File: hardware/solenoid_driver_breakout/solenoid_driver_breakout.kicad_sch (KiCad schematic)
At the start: 24 parts, among them J1 DC IN, J2 CONTROL, J3 Solenoid, Q1 PMV40UN2R, Q2 PMV40UN2R

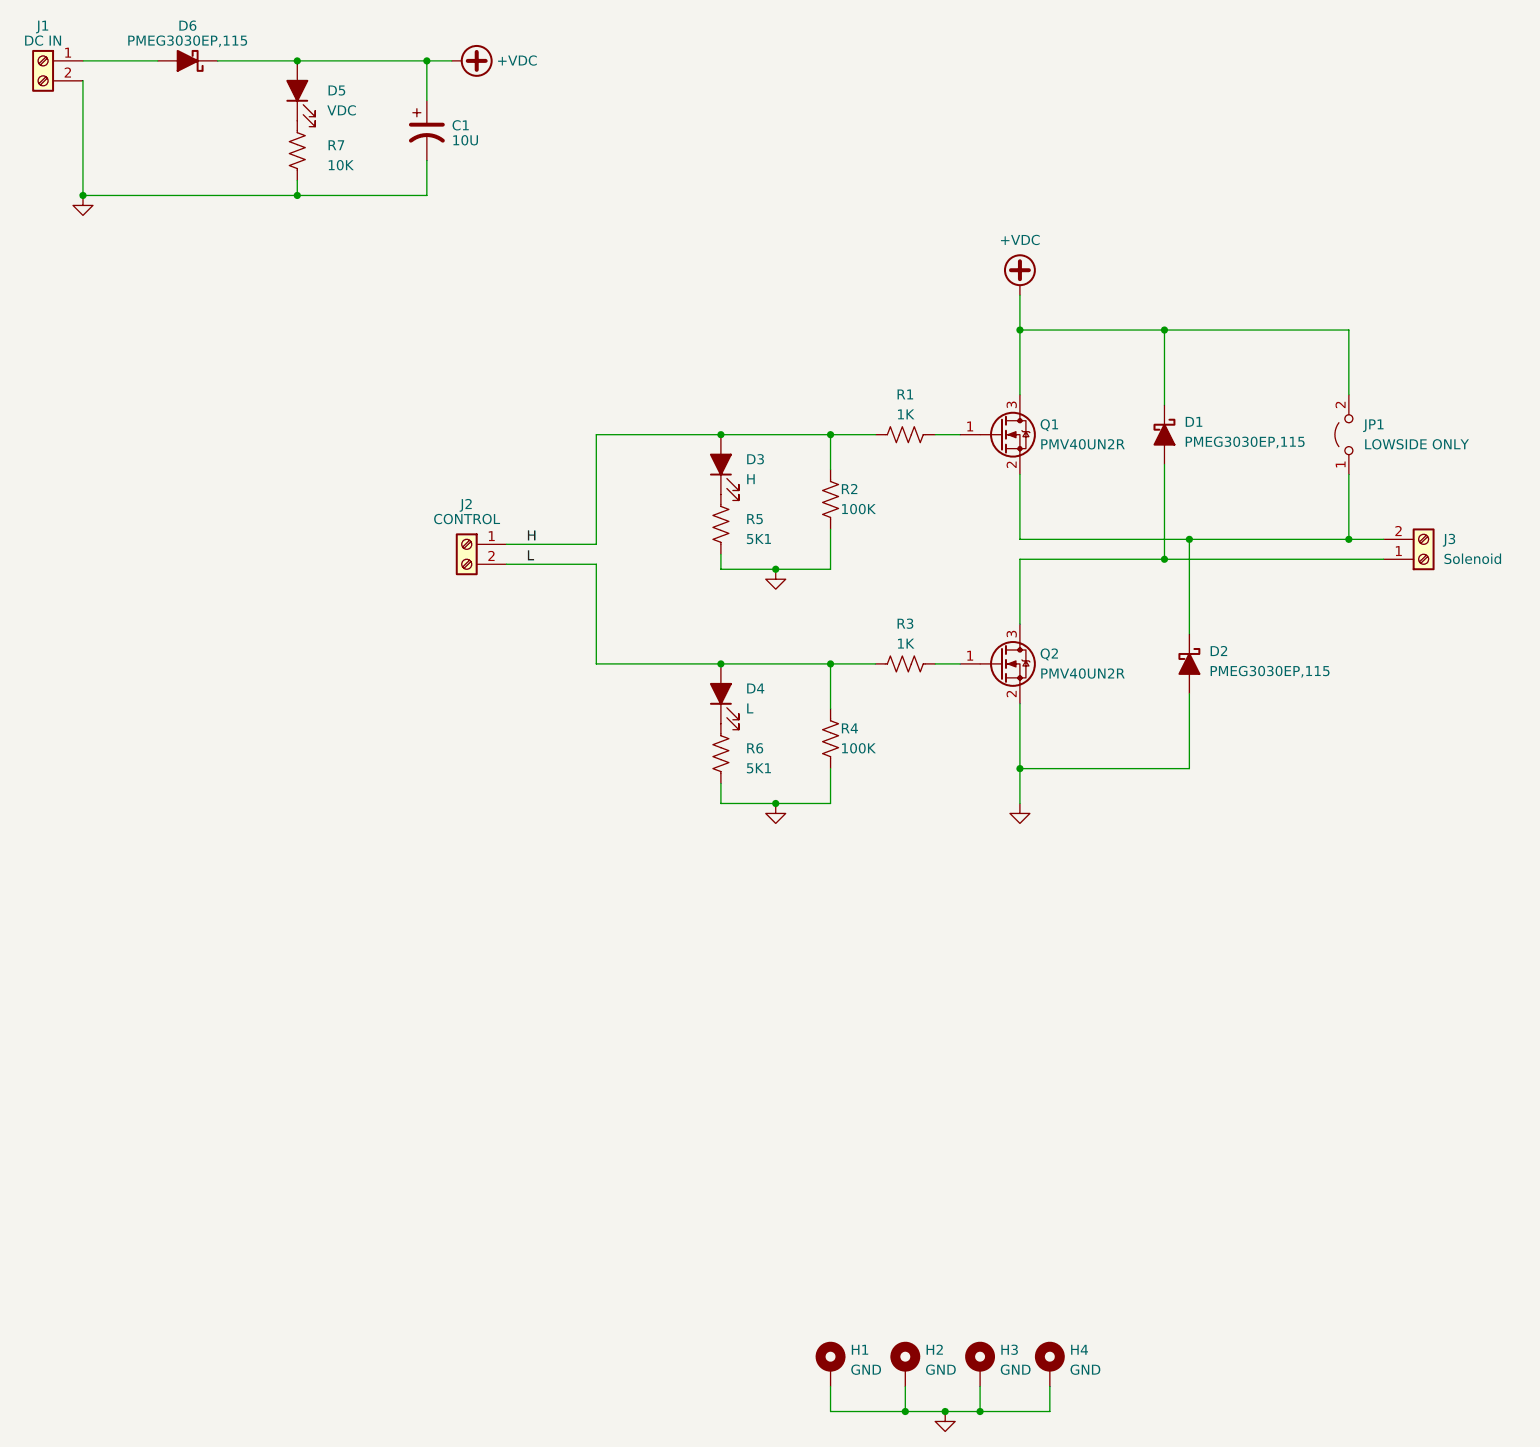
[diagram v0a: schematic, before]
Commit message: Switch solenoid driver to dual low-side switches
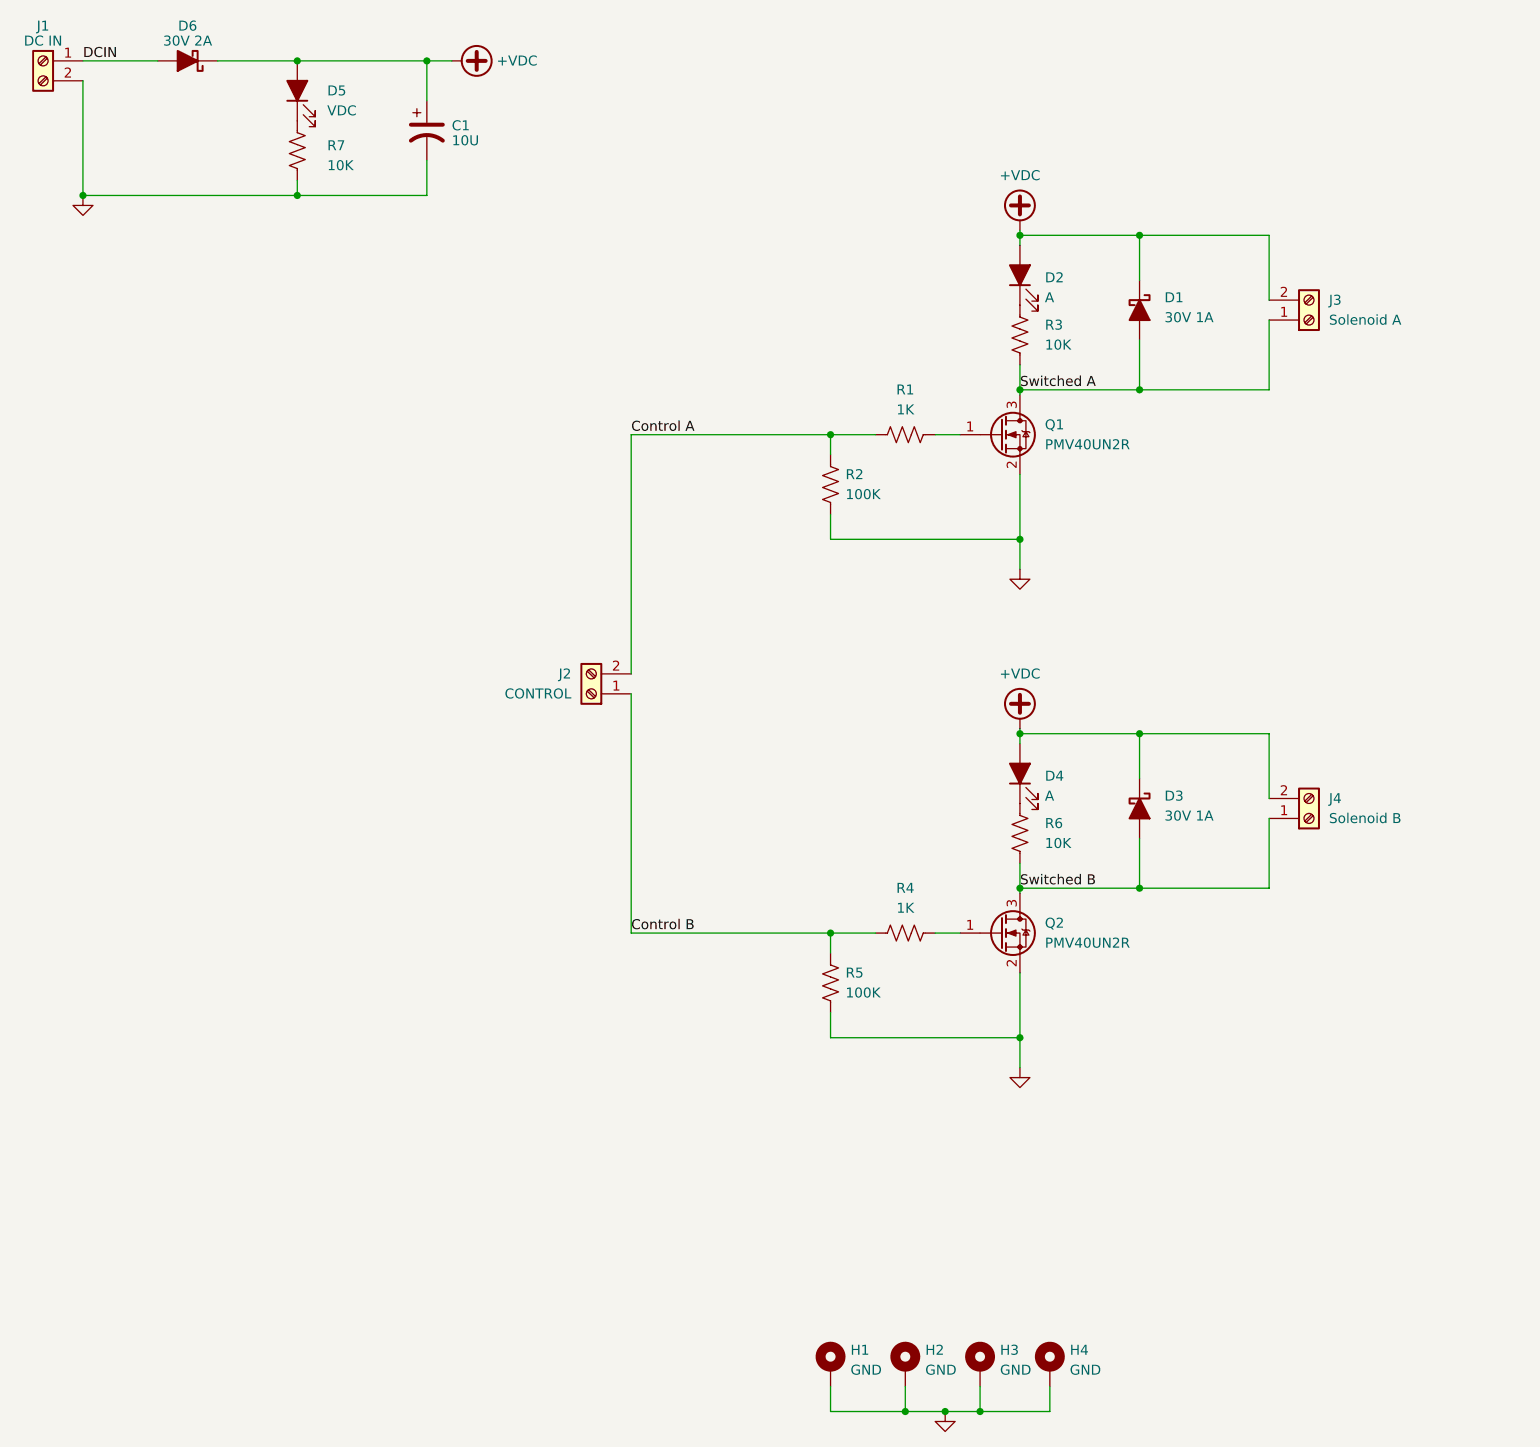
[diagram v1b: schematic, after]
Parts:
- removed D2: PMEG3030EP,115, Diode_SMD:D_SOD-128, symbol Device:D_Schottky_Filled
- removed JP1: LOWSIDE ONLY, Jumper:SolderJumper-2_P1.3mm_Open_Pad1.0x1.5mm, symbol Jumper:Jumper_2_Open
- removed R3: 1K, Resistor_SMD:R_0603_1608Metric_Pad0.98x0.95mm_HandSolder, symbol Device:R_US
- added D3: 30V 1A, Diode_SMD:D_SOD-128, symbol Device:D_Schottky_Filled
- added J4: Solenoid B, winterbloom:TerminalBlock_4UCON_1x02_P3.50mm_Horizontal, symbol Connector:Screw_Terminal_01x02
- added R5: 100K, Resistor_SMD:R_0603_1608Metric_Pad0.98x0.95mm_HandSolder, symbol Device:R_US
- D1: value PMEG3030EP,115 -> 30V 1A
- D2: renamed from D3; value H -> A
- D4: value L -> A
- D6: value PMEG3030EP,115 -> 30V 2A
- J3: value Solenoid -> Solenoid A
- R3: renamed from R5; value 5K1 -> 10K
- R4: value 100K -> 1K
- R6: value 5K1 -> 10K
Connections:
- net +VDC: now also D2.2 (A), D4.2 (A), J3.2 (Pin_2), D3.1 (K), J4.2 (Pin_2); no longer Q1.3 (D)
- net GND: now also Q1.2 (S), R5.2; no longer R3.2, R4.2, R6.2
- net at Q2.1 (G): now also R4.2
- net Switched A: now reaches D1.2 (A), J3.1 (Pin_1)
- net Switched A: now also Q1.3 (D), R3.2; no longer Q2.3 (D)
- net DCIN: now reaches D6.2 (A), J1.1 (Pin_1)
- net H renamed Control A
- net Control A: now also J2.2 (Pin_2); no longer D2.2 (A), J2.1 (Pin_1)
- removed net L: D4.2 (A), J2.2 (Pin_2), R4.1
- new net Control B: J2.1 (Pin_1), R4.1, R5.1
- new net Switched B: D3.2 (A), J4.1 (Pin_1), Q2.3 (D), R6.2
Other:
- moved on the sheet: D1, D2, J2, J3, R2, R3
